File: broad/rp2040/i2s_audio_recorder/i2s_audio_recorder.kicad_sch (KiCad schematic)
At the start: 55 parts, among them J1 USB_C_Receptacle_USB2.0_16P, J2 Conn_01x04_Pin, J3 SD_Card_Device, J4 Conn_01x08_Pin, J5 Conn_01x08_Pin, J6 Conn_01x08_Pin, SW1 TS342A2P-WZ, SW2 TS342A2P-WZ, SW3 TS342A2P-WZ, SW4 TS342A2P-WZ, U1 MSM261S4030H0R, U1 SMBJ5.0CA, U2 RP2040, U3 SMBJ5.0CA, U4 SMBJ5.0CA, U5 AMS1117-3.3, U7 W25Q128JVS, Y1 12M

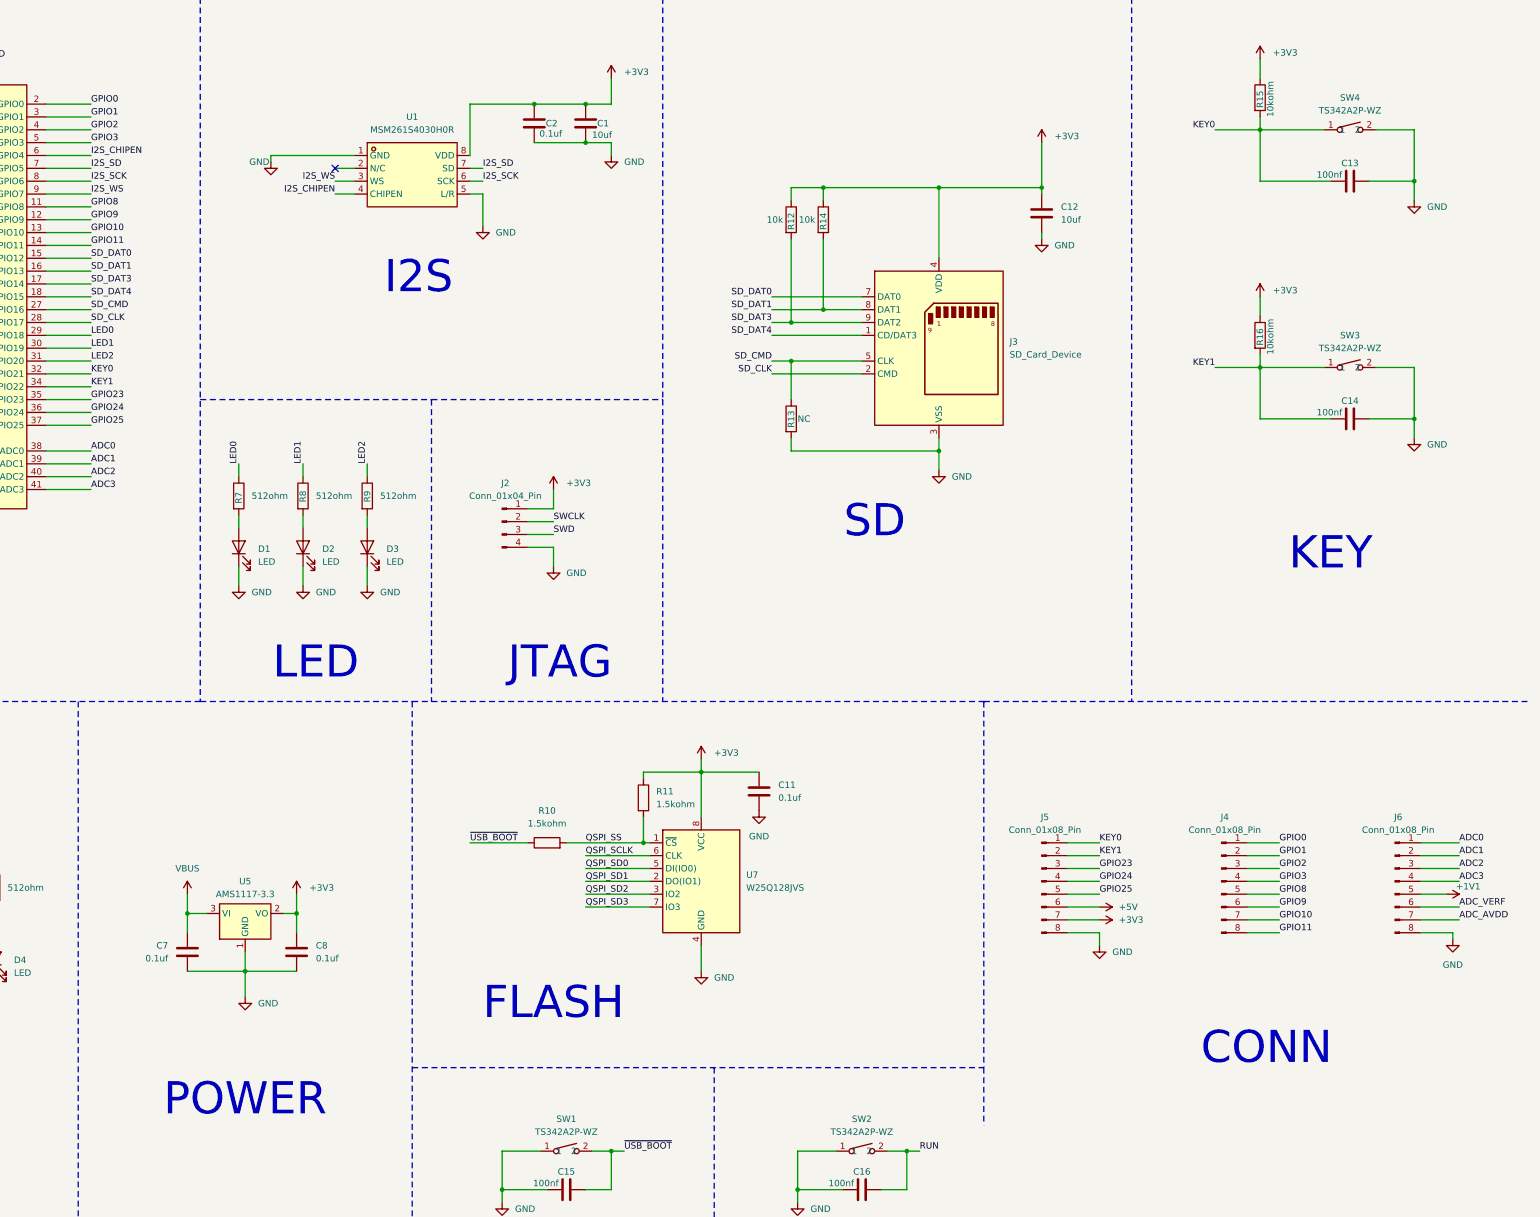
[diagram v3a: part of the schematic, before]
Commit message: Finish basic layout of `i2s_audio_recorder`
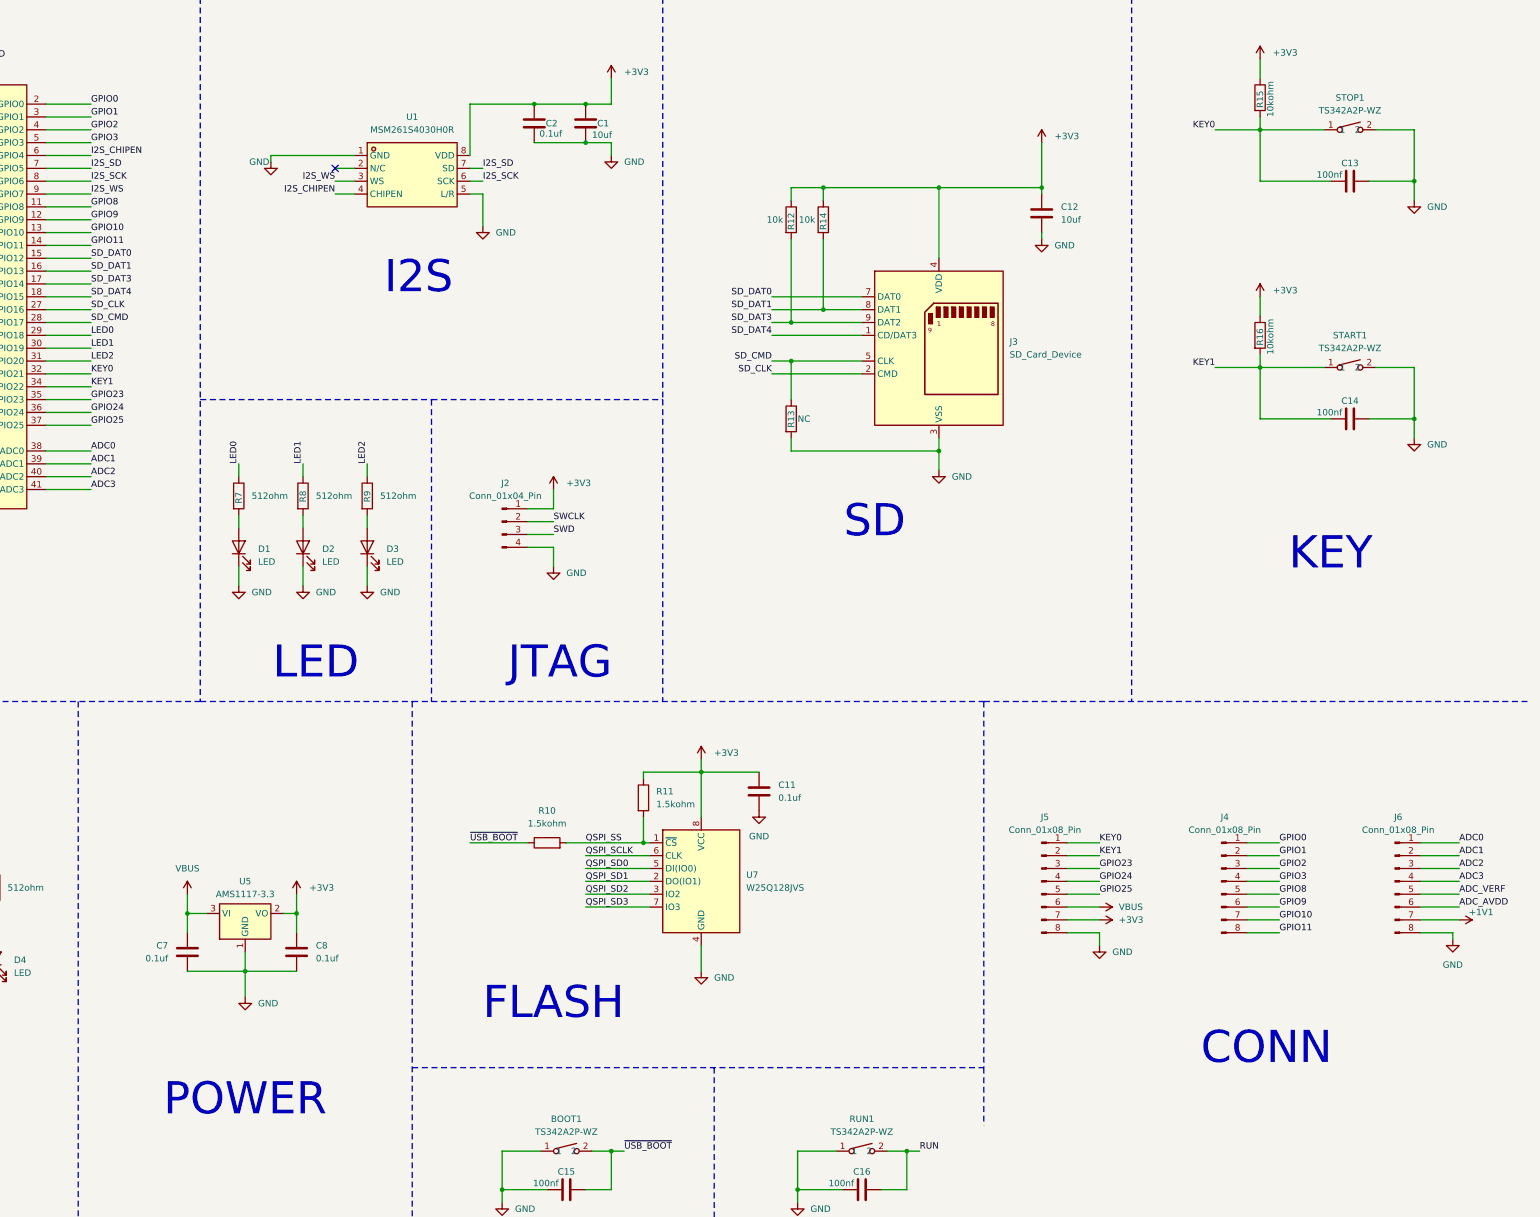
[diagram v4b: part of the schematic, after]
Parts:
- D1, D2, D3, D4: footprint Capacitor_SMD:C_0603_1608Metric -> LED_SMD:LED_0603_1608Metric_Pad1.05x0.95mm_HandSolder
- renumbered SW1 to BOOT1, SW2 to RUN1, SW3 to START1, SW4 to STOP1
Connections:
- net +5V is gone; now on net VBUS: J5.6 (Pin_6)
- net +1V1: now also J6.7 (Pin_7); no longer J6.5 (Pin_5)
- net ADC_AVDD: now also J6.6 (Pin_6); no longer J6.7 (Pin_7)
- net ADC_VERF: now also J6.5 (Pin_5); no longer J6.6 (Pin_6)
- net SD_CLK: now also U2.27 (GPIO16); no longer U2.28 (GPIO17)
- net SD_CMD: now also U2.28 (GPIO17); no longer U2.27 (GPIO16)
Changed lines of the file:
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@@
 	(wire
 		(pts
-			(xy 391.16 207.01) (xy 386.08 207.01)
+			(xy 386.08 207.01) (xy 393.7 207.01)
 		)
 		(stroke
@@
 		)
 	)
-	(label "ADC_VERF"
-		(at 393.7 209.55 0)
-		(fields_autoplaced yes)
-		(effects
-			(font
-				(size 1.27 1.27)
-			)
-			(justify left bottom)
-		)
-	)
 	(label "SD_DAT1"
 		(at 123.19 83.82 0)
@@
 		)
 	)
-	(label "SD_CLK"
-		(at 123.19 93.98 0)
-		(fields_autoplaced yes)
-		(effects
-			(font
-				(size 1.27 1.27)
-			)
-			(justify left bottom)
-		)
-	)
 	(label "GPIO1"
 		(at 123.19 53.34 0)
@@
 		)
 	)
+	(label "ADC_VERF"
+		(at 393.7 207.01 0)
+		(fields_autoplaced yes)
+		(effects
+			(font
+				(size 1.27 1.27)
+			)
+			(justify left bottom)
+		)
+	)
 	(label "ADC_AVDD"
-		(at 393.7 212.09 0)
+		(at 393.7 209.55 0)
 		(fields_autoplaced yes)
 		(effects
@@
 		)
 	)
+	(label "SD_CLK"
+		(at 123.19 91.44 0)
+		(fields_autoplaced yes)
+		(effects
+			(font
+				(size 1.27 1.27)
+			)
+			(justify left bottom)
+		)
+	)
 	(label "GPIO1"
 		(at 358.14 199.39 0)
@@
 		)
 	)
-	(label "SD_CMD"
-		(at 123.19 91.44 0)
-		(fields_autoplaced yes)
-		(effects
-			(font
-				(size 1.27 1.27)
-			)
-			(justify left bottom)
-		)
-	)
 	(label "I2S_WS"
 		(at 171.45 66.04 180)
@@
 		)
 	)
+	(label "SD_CMD"
+		(at 123.19 93.98 0)
+		(fields_autoplaced yes)
+		(effects
+			(font
+				(size 1.27 1.27)
+			)
+			(justify left bottom)
+		)
+	)
 	(label "I2S_WS"
 		(at 123.19 68.58 0)
@@
 	)
 	(symbol
-		(lib_id "power:+1V1")
-		(at 391.16 207.01 270)
-		(unit 1)
-		(exclude_from_sim no)
-		(in_bom yes)
-		(on_board yes)
-		(dnp no)
-		(fields_autoplaced yes)
-		(property "Reference" "#PWR038"
-			(at 387.35 207.01 0)
-			(effects
-				(font
-					(size 1.27 1.27)
-				)
-				(hide yes)
-			)
-		)
-		(property "Value" "+1V1"
-			(at 395.478 205.486 90)
-			(do_not_autoplace yes)
-			(effects
-				(font
-					(size 1.27 1.27)
-				)
-			)
-		)
-		(property "Footprint" ""
-			(at 391.16 207.01 0)
-			(effects
-				(font
-					(size 1.27 1.27)
-				)
-				(hide yes)
-			)
-		)
-		(property "Datasheet" ""
-			(at 391.16 207.01 0)
-			(effects
-				(font
-					(size 1.27 1.27)
-				)
-				(hide yes)
-			)
-		)
-		(property "Description" "Power symbol creates a global label with name \"+1V1\""
-			(at 391.16 207.01 0)
-			(effects
-				(font
-					(size 1.27 1.27)
-				)
-				(hide yes)
-			)
-		)
-		(pin "1"
-		)
-		(instances
-			(project "audio"
-				(path "/686bcb0d-1b9d-4fec-a21a-3860a78c3874"
-					(reference "#PWR038")
-					(unit 1)
-				)
-			)
-		)
-	)
-	(symbol
 		(lib_id "Connector:USB_C_Receptacle_USB2.0_16P")
 		(at 33.02 214.63 0)
@@
 	)
 	(symbol
+		(lib_id "power:VBUS")
+		(at 322.58 209.55 270)
+		(unit 1)
+		(exclude_from_sim no)
+		(in_bom yes)
+		(on_board yes)
+		(dnp no)
+		(fields_autoplaced yes)
+		(property "Reference" "#PWR037"
+			(at 318.77 209.55 0)
+			(effects
+				(font
+					(size 1.27 1.27)
+				)
+				(hide yes)
+			)
+		)
+		(property "Value" "VBUS"
+			(at 326.39 209.5499 90)
+			(effects
+				(font
+					(size 1.27 1.27)
+				)
+				(justify left)
+			)
+		)
+		(property "Footprint" ""
+			(at 322.58 209.55 0)
+			(effects
+				(font
+					(size 1.27 1.27)
+				)
+				(hide yes)
+			)
+		)
+		(property "Datasheet" ""
+			(at 322.58 209.55 0)
+			(effects
+				(font
+					(size 1.27 1.27)
+				)
+				(hide yes)
+			)
+		)
+		(property "Description" "Power symbol creates a global label with name \"VBUS\""
+			(at 322.58 209.55 0)
+			(effects
+				(font
+					(size 1.27 1.27)
+				)
+				(hide yes)
+			)
+		)
+		(pin "1"
+		)
+		(instances
+			(project "i2s_audio_recorder"
+				(path "/686bcb0d-1b9d-4fec-a21a-3860a78c3874"
+					(reference "#PWR037")
+					(unit 1)
+				)
+			)
+		)
+	)
+	(symbol
 		(lib_id "power:PWR_FLAG")
 		(at 66.04 199.39 0)
@@
 			)
 		)
-		(property "Footprint" "Capacitor_SMD:C_0603_1608Metric"
+		(property "Footprint" "LED_SMD:LED_0603_1608Metric_Pad1.05x0.95mm_HandSolder"
 			(at 165.1 138.43 0)
 			(effects
@@
 			)
 		)
-		(property "Footprint" "Capacitor_SMD:C_0603_1608Metric"
+		(property "Footprint" "LED_SMD:LED_0603_1608Metric_Pad1.05x0.95mm_HandSolder"
 			(at 104.14 219.71 0)
 			(effects
@@
 		(dnp no)
 		(fields_autoplaced yes)
-		(property "Reference" "SW2"
+		(property "Reference" "RUN1"
 			(at 275.59 251.46 0)
 			(effects
@@
 			(project "i2s_audio_recorder"
 				(path "/686bcb0d-1b9d-4fec-a21a-3860a78c3874"
-					(reference "SW2")
+					(reference "RUN1")
 					(unit 1)
 				)
@@
 		(dnp no)
 		(fields_autoplaced yes)
-		(property "Reference" "SW1"
+		(property "Reference" "BOOT1"
 			(at 217.17 251.46 0)
 			(effects
@@
 			(project ""
 				(path "/686bcb0d-1b9d-4fec-a21a-3860a78c3874"
-					(reference "SW1")
+					(reference "BOOT1")
 					(unit 1)
 				)
@@
 	)
 	(symbol
-		(lib_id "power:+5V")
-		(at 322.58 209.55 270)
-		(unit 1)
-		(exclude_from_sim no)
-		(in_bom yes)
-		(on_board yes)
-		(dnp no)
-		(fields_autoplaced yes)
-		(property "Reference" "#PWR037"
-			(at 318.77 209.55 0)
-			(effects
-				(font
-					(size 1.27 1.27)
-				)
-				(hide yes)
-			)
-		)
-		(property "Value" "+5V"
-			(at 326.39 209.5499 90)
-			(effects
-				(font
-					(size 1.27 1.27)
-				)
-				(justify left)
-			)
-		)
-		(property "Footprint" ""
-			(at 322.58 209.55 0)
-			(effects
-				(font
-					(size 1.27 1.27)
-				)
-				(hide yes)
-			)
-		)
-		(property "Datasheet" ""
-			(at 322.58 209.55 0)
-			(effects
-				(font
-					(size 1.27 1.27)
-				)
-				(hide yes)
-			)
-		)
-		(property "Description" "Power symbol creates a global label with name \"+5V\""
-			(at 322.58 209.55 0)
-			(effects
-				(font
-					(size 1.27 1.27)
-				)
-				(hide yes)
-			)
-		)
-		(pin "1"
-		)
-		(instances
-			(project ""
-				(path "/686bcb0d-1b9d-4fec-a21a-3860a78c3874"
-					(reference "#PWR037")
-					(unit 1)
-				)
-			)
-		)
-	)
-	(symbol
 		(lib_id "Device:R")
 		(at 267.97 73.66 0)
@@
 		(dnp no)
 		(fields_autoplaced yes)
-		(property "Reference" "SW4"
+		(property "Reference" "STOP1"
 			(at 372.11 49.53 0)
 			(effects
@@
 			(project "i2s_audio_recorder"
 				(path "/686bcb0d-1b9d-4fec-a21a-3860a78c3874"
-					(reference "SW4")
+					(reference "STOP1")
+					(unit 1)
+				)
+			)
+		)
+	)
+	(symbol
+		(lib_id "power:+1V1")
+		(at 393.7 212.09 270)
+		(unit 1)
+		(exclude_from_sim no)
+		(in_bom yes)
+		(on_board yes)
+		(dnp no)
+		(fields_autoplaced yes)
+		(property "Reference" "#PWR038"
+			(at 389.89 212.09 0)
+			(effects
+				(font
+					(size 1.27 1.27)
+				)
+				(hide yes)
+			)
+		)
+		(property "Value" "+1V1"
+			(at 398.018 210.566 90)
+			(do_not_autoplace yes)
+			(effects
+				(font
+					(size 1.27 1.27)
+				)
+			)
+		)
+		(property "Footprint" ""
+			(at 393.7 212.09 0)
+			(effects
+				(font
+					(size 1.27 1.27)
+				)
+				(hide yes)
+			)
+		)
+		(property "Datasheet" ""
+			(at 393.7 212.09 0)
+			(effects
+				(font
+					(size 1.27 1.27)
+				)
+				(hide yes)
+			)
+		)
+		(property "Description" "Power symbol creates a global label with name \"+1V1\""
+			(at 393.7 212.09 0)
+			(effects
+				(font
+					(size 1.27 1.27)
+				)
+				(hide yes)
+			)
+		)
+		(pin "1"
+		)
+		(instances
+			(project "i2s_audio_recorder"
+				(path "/686bcb0d-1b9d-4fec-a21a-3860a78c3874"
+					(reference "#PWR038")
 					(unit 1)
 				)
@@
 			)
 		)
-		(property "Footprint" "Capacitor_SMD:C_0603_1608Metric"
+		(property "Footprint" "LED_SMD:LED_0603_1608Metric_Pad1.05x0.95mm_HandSolder"
 			(at 177.8 138.43 0)
 			(effects
@@
 			)
 		)
-		(property "Footprint" "Capacitor_SMD:C_0603_1608Metric"
+		(property "Footprint" "LED_SMD:LED_0603_1608Metric_Pad1.05x0.95mm_HandSolder"
 			(at 152.4 138.43 0)
 			(effects
@@
 		(dnp no)
 		(fields_autoplaced yes)
-		(property "Reference" "SW3"
+		(property "Reference" "START1"
 			(at 372.11 96.52 0)
 			(effects
@@
 			(project "i2s_audio_recorder"
 				(path "/686bcb0d-1b9d-4fec-a21a-3860a78c3874"
-					(reference "SW3")
+					(reference "START1")
 					(unit 1)
 				)

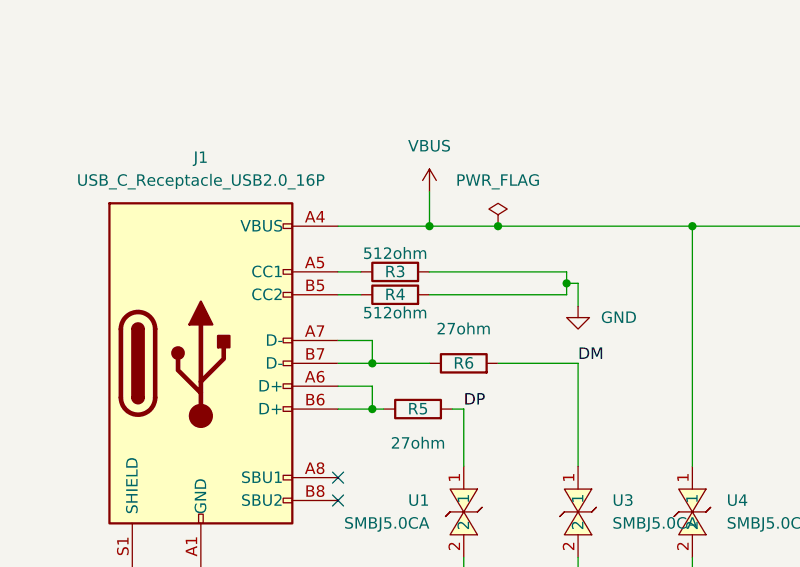
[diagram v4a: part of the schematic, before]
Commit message: Change `i2s_audio_recorder` R3 R4 from `512 ohm` to `5.1k ohm`
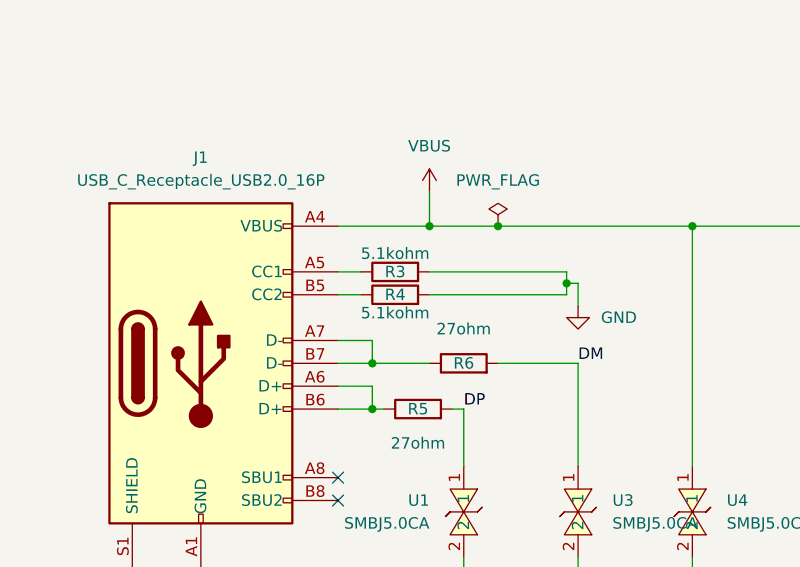
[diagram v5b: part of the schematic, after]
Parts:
- R3, R4: value 512ohm -> 5.1kohm
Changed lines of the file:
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@@
 			)
 		)
-		(property "Value" "512ohm"
+		(property "Value" "5.1kohm"
 			(at 54.61 209.042 90)
 			(do_not_autoplace yes)
@@
 			)
 		)
-		(property "Value" "512ohm"
+		(property "Value" "5.1kohm"
 			(at 54.61 202.438 90)
 			(do_not_autoplace yes)

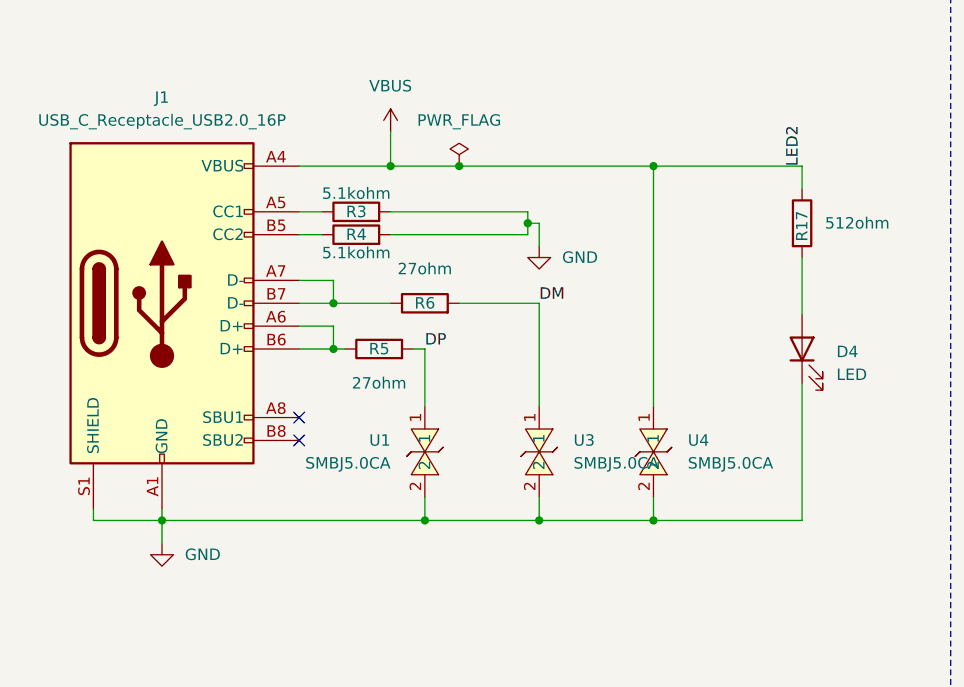
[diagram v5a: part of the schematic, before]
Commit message: Re-layout of the TVS position of `i2s_audio_recorder`
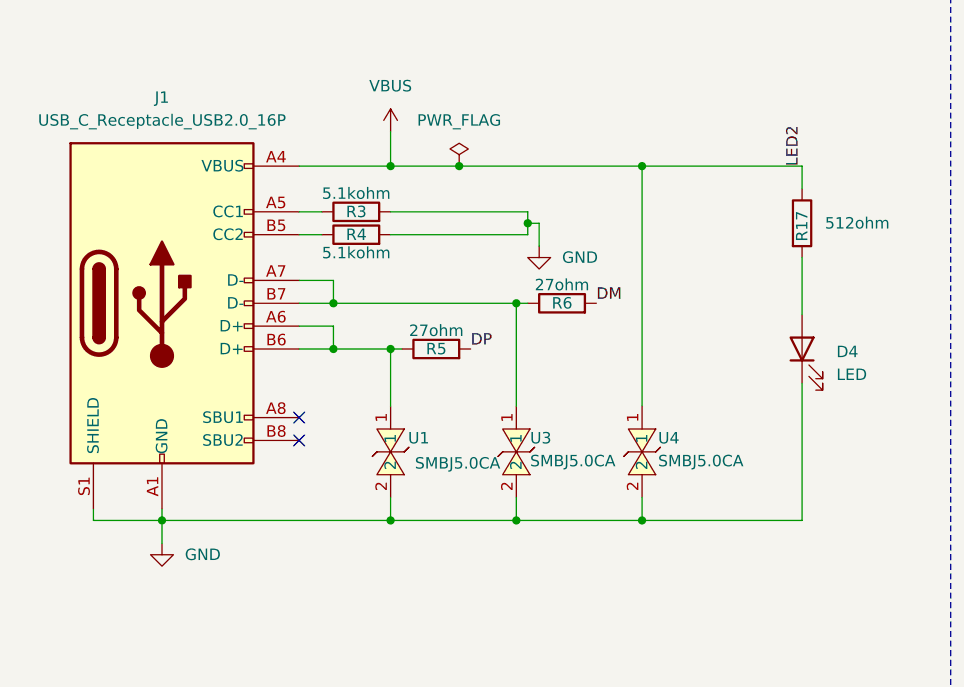
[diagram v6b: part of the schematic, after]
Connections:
- net DM: no longer U3.1
- net DP: no longer U1.1
- net at J1.A6 (D+), J1.B6 (D+), R5.1: now also U1.1
- net at J1.A7 (D-), J1.B7 (D-), R6.1: now also U3.1
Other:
- moved on the sheet: U1, U3, U4
